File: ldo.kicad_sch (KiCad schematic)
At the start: 4 parts, among them U501 SPX3819M5-L-3-3

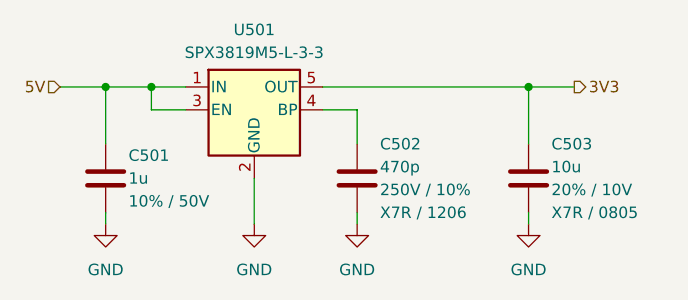
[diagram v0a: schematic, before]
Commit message: Switch to 16 pin USB-C
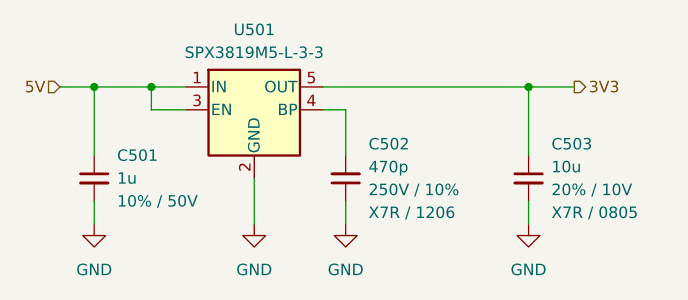
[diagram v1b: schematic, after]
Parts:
- C501, C502, C503: symbol Device:C -> Device:C_Small
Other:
- moved on the sheet: C501, C502

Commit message: Correct SPI pinout
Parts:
- C501: Dielectric (none) -> X7R; Line 2 (none) -> ${Dielectric} / ${Package}
- C502: value 470p -> 10n; footprint Capacitor_SMD:C_1206_3216Metric -> Capacitor_SMD:C_0603_1608Metric; LCSC Part Number C107212 -> C100042; MPN CC1206KRX7RYBB471 -> CC0603KRX7R9BB103; Package 1206 -> 0603; Rated Voltage 250V -> 50V
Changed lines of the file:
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@@
 			)
 		)
-		(property "Description" ""
+		(property "Description" "Power symbol creates a global label with name \"GND\" , ground"
 			(at 93.98 76.2 0)
 			(effects
@@
 			)
 		)
-		(property "Description" ""
+		(property "Description" "Unpolarized capacitor, small symbol"
 			(at 66.04 71.12 0)
 			(effects
@@
 			)
 		)
-		(property "Line 2" ""
-			(at 66.04 71.12 0)
-			(effects
-				(font
-					(size 1.27 1.27)
-				)
+		(property "Line 2" "${Dielectric} / ${Package}"
+			(at 68.834 76.2 0)
+			(effects
+				(font
+					(size 1.27 1.27)
+				)
+				(justify left)
 			)
 		)
@@
 		)
 		(property "Rated Voltage" "50V"
+			(at 66.04 71.12 0)
+			(effects
+				(font
+					(size 1.27 1.27)
+				)
+				(hide yes)
+			)
+		)
+		(property "Dielectric" "X7R"
 			(at 66.04 71.12 0)
 			(effects
@@
 			)
 		)
-		(property "Description" ""
+		(property "Description" "Power symbol creates a global label with name \"GND\" , ground"
 			(at 114.3 76.2 0)
 			(effects
@@
 			)
 		)
-		(property "Description" ""
+		(property "Description" "500mA Low drop-out regulator, Fixed Output 3.3V, SOT-23-5"
 			(at 83.82 63.5 0)
 			(effects
@@
 			)
 		)
-		(property "Value" "470p"
+		(property "Value" "10n	"
 			(at 96.52 69.85 0)
 			(effects
@@
 			)
 		)
-		(property "Footprint" "Capacitor_SMD:C_1206_3216Metric"
+		(property "Footprint" "Capacitor_SMD:C_0603_1608Metric"
 			(at 93.98 71.12 0)
 			(effects
@@
 			)
 		)
-		(property "Description" ""
+		(property "Description" "Unpolarized capacitor, small symbol"
 			(at 93.98 71.12 0)
 			(effects
@@
 			)
 		)
-		(property "LCSC Part Number" "C107212"
+		(property "LCSC Part Number" "C100042"
 			(at 93.98 71.12 0)
 			(effects
@@
 			)
 		)
-		(property "MPN" "CC1206KRX7RYBB471"
+		(property "MPN" "CC0603KRX7R9BB103"
 			(at 93.98 71.12 0)
 			(effects
@@
 			)
 		)
-		(property "Package" "1206"
-			(at 93.98 71.12 0)
-			(effects
-				(font
-					(size 1.27 1.27)
-				)
-				(hide yes)
-			)
-		)
-		(property "Rated Voltage" "250V"
+		(property "Package" "0603"
+			(at 93.98 71.12 0)
+			(effects
+				(font
+					(size 1.27 1.27)
+				)
+				(hide yes)
+			)
+		)
+		(property "Rated Voltage" "50V"
 			(at 93.98 71.12 0)
 			(effects
@@
 			)
 		)
-		(property "Description" ""
+		(property "Description" "Unpolarized capacitor, small symbol"
 			(at 114.3 71.12 0)
 			(effects
@@
 			)
 		)
-		(property "Description" ""
+		(property "Description" "Power symbol creates a global label with name \"GND\" , ground"
 			(at 66.04 76.2 0)
 			(effects
@@
 			)
 		)
-		(property "Description" ""
+		(property "Description" "Power symbol creates a global label with name \"GND\" , ground"
 			(at 83.82 76.2 0)
 			(effects

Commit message: Finish everything
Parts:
- U501: LCSC Part Number (none) -> C9055; MPN (none) -> SPX3819M5-L-3-3/TR; Manufacturer (none) -> MaxLinear
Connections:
- net BYP: now reaches C502.2, U501.4 (BP)
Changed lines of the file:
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@@
+		)
+	)
+	(label "BYP"
+		(at 93.98 63.5 0)
+		(fields_autoplaced yes)
+		(effects
+			(font
+				(size 1.27 1.27)
+			)
+			(justify left bottom)
 		)
 	)
@@
 			(at 83.82 63.5 0)
 			(effects
+				(font
+					(size 1.27 1.27)
+				)
+				(hide yes)
+			)
+		)
+		(property "LCSC Part Number" "C9055"
+			(at 83.82 63.5 0)
+			(effects
+				(font
+					(size 1.27 1.27)
+				)
+				(hide yes)
+			)
+		)
+		(property "MPN" "SPX3819M5-L-3-3/TR "
+			(at 83.82 63.5 0)
+			(effects
+				(font
+					(size 1.27 1.27)
+				)
+				(hide yes)
+			)
+		)
+		(property "Manufacturer" "MaxLinear"
+			(at 83.82 63.5 0)
+			(effects
